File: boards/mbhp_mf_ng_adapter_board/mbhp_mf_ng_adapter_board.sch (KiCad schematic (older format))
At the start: 12 parts, among them J1 Analog Inputs, J2 Power, U1 NodeMCU_ESP32, U2 MCP3208, U3 PIC18FAdapter

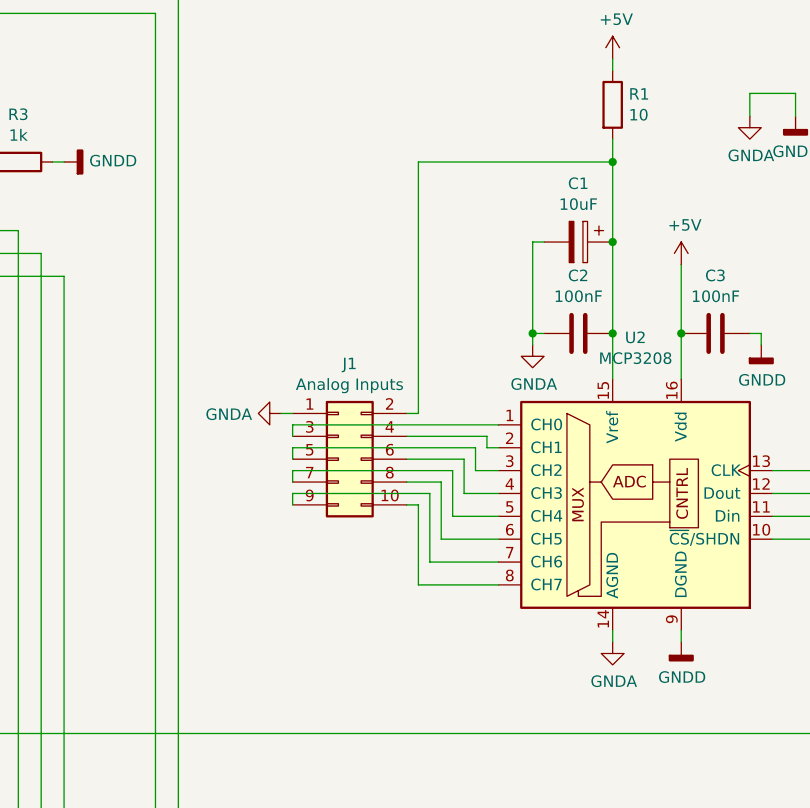
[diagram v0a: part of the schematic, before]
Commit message: Adaptor prototype ready for OSHpark
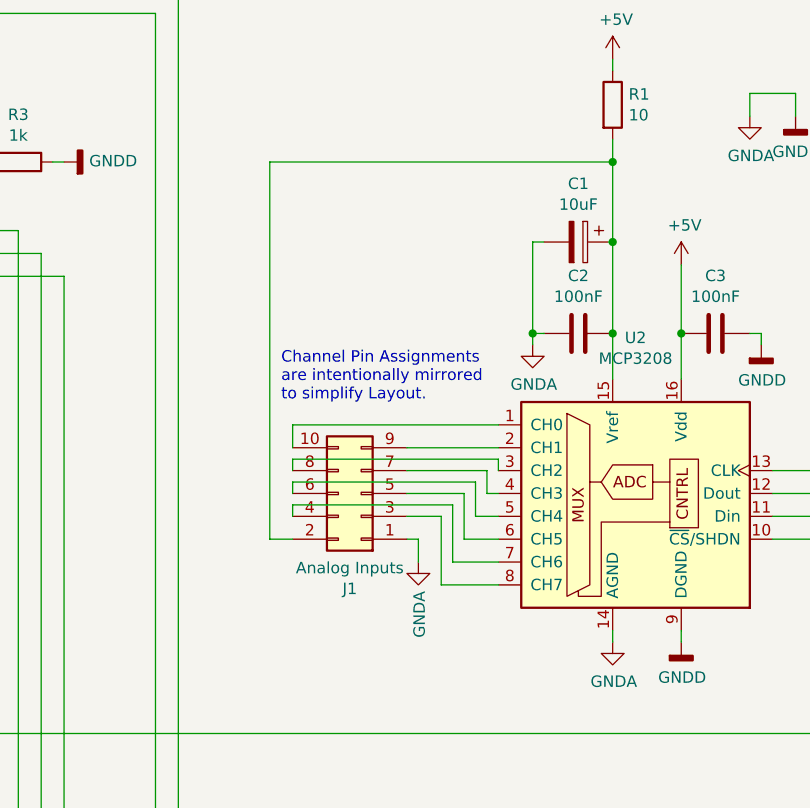
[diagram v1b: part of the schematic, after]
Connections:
- net at U2.1 (CH0): now also J1.10 (Pin_10); no longer J1.3 (Pin_3)
- net at U2.2 (CH1): now also J1.9 (Pin_9); no longer J1.4 (Pin_4)
- net at U2.3 (CH2): now also J1.8 (Pin_8); no longer J1.5 (Pin_5)
- net at U2.4 (CH3): now also J1.7 (Pin_7); no longer J1.6 (Pin_6)
- net at U2.5 (CH4): now also J1.6 (Pin_6); no longer J1.7 (Pin_7)
- net at U2.6 (CH5): now also J1.5 (Pin_5); no longer J1.8 (Pin_8)
- net at U2.7 (CH6): now also J1.4 (Pin_4); no longer J1.9 (Pin_9)
- net at U2.8 (CH7): now also J1.3 (Pin_3); no longer J1.10 (Pin_10)
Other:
- note added: "Channel Pin Assignments\nare intentionally mirrored\nto simplify Layout."
- moved on the sheet: J1
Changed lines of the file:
@@
 Text Label 4450 4050 0    50   ~ 0
 SPI_MISO_DINSR
-Wire Wire Line
-	7550 3150 7550 3500
-Wire Wire Line
-	7500 3150 7550 3150
-Wire Wire Line
-	7600 3100 7600 3400
-Wire Wire Line
-	7000 3100 7600 3100
-Wire Wire Line
-	7000 3150 7000 3100
-Wire Wire Line
-	7650 3050 7650 3300
-Wire Wire Line
-	7500 3050 7650 3050
-Wire Wire Line
-	7700 3000 7700 3200
-Wire Wire Line
-	7000 3000 7700 3000
-Wire Wire Line
-	7000 3050 7000 3000
-Wire Wire Line
-	7750 2950 7750 3100
-Wire Wire Line
-	7500 2950 7750 2950
-Wire Wire Line
-	7800 2900 7800 3000
-Wire Wire Line
-	7000 2900 7800 2900
-Wire Wire Line
-	7000 2950 7000 2900
-Wire Wire Line
-	7500 2850 7850 2850
-Wire Wire Line
-	7000 2800 7000 2850
 $Comp
 L Connector_Generic:Conn_02x05_Odd_Even J1
 U 1 1 5E140616
-P 7200 2950
-F 0 "J1" H 7250 3367 50  0000 C CNN
-F 1 "Analog Inputs" H 7250 3276 50  0000 C CNN
-F 2 "Connector_IDC:IDC-Header_2x05_P2.54mm_Vertical" H 7200 2950 50  0001 C CNN
-F 3 "~" H 7200 2950 50  0001 C CNN
-	1    7200 2950
-	1    0    0    -1
+P 7300 3100
+F 0 "J1" H 7350 3517 50  0000 C CNN
+F 1 "Analog Inputs" H 7350 3426 50  0000 C CNN
+F 2 "Connector_IDC:IDC-Header_2x05_P2.54mm_Vertical" H 7300 3100 50  0001 C CNN
+F 3 "~" H 7300 3100 50  0001 C CNN
+	1    7300 3100
+	-1   0    0    1
 $EndComp
 $Comp
 L power:GNDA #PWR01
 U 1 1 5E142455
-P 6950 2750
-F 0 "#PWR01" H 6950 2500 50  0001 C CNN
-F 1 "GNDA" V 6955 2623 50  0000 R CNN
-F 2 "" H 6950 2750 50  0001 C CNN
-F 3 "" H 6950 2750 50  0001 C CNN
-	1    6950 2750
-	0    1    1    0
+P 7550 3400
+F 0 "#PWR01" H 7550 3150 50  0001 C CNN
+F 1 "GNDA" V 7555 3273 50  0000 R CNN
+F 2 "" H 7550 3400 50  0001 C CNN
+F 3 "" H 7550 3400 50  0001 C CNN
+	1    7550 3400
+	1    0    0    -1
 $EndComp
-Wire Wire Line
-	6950 2750 7000 2750
-Wire Wire Line
-	7500 2750 7550 2750
-Wire Wire Line
-	7000 2800 7900 2800
-Wire Wire Line
-	7850 2850 7850 2900
-Wire Wire Line
-	7850 2900 7900 2900
-Wire Wire Line
-	7800 3000 7900 3000
-Wire Wire Line
-	7750 3100 7900 3100
-Wire Wire Line
-	7700 3200 7900 3200
-Wire Wire Line
-	7650 3300 7900 3300
-Wire Wire Line
-	7600 3400 7900 3400
-Wire Wire Line
-	7550 3500 7900 3500
 Text GLabel 5250 4750 2    50   Input ~ 0
 MIDI_TX
@@
 Wire Wire Line
 	8400 1550 8400 1650
-Wire Wire Line
-	7550 2750 7550 1650
-Wire Wire Line
-	7550 1650 8400 1650
 Connection ~ 8400 1650
 Wire Wire Line
 	8400 1650 8400 2000
+Wire Wire Line
+	7000 2900 7000 2800
+Wire Wire Line
+	7000 2800 7900 2800
+Wire Wire Line
+	7500 2900 7900 2900
+Wire Wire Line
+	7000 3000 7000 2950
+Wire Wire Line
+	7000 2950 7900 2950
+Wire Wire Line
+	7900 2950 7900 3000
+Wire Wire Line
+	7500 3000 7850 3000
+Wire Wire Line
+	7850 3000 7850 3100
+Wire Wire Line
+	7850 3100 7900 3100
+Wire Wire Line
+	7000 3100 7000 3050
+Wire Wire Line
+	7000 3050 7800 3050
+Wire Wire Line
+	7800 3050 7800 3200
+Wire Wire Line
+	7800 3200 7900 3200
+Wire Wire Line
+	7500 3100 7750 3100
+Wire Wire Line
+	7750 3100 7750 3300
+Wire Wire Line
+	7750 3300 7900 3300
+Wire Wire Line
+	7000 3200 7000 3150
+Wire Wire Line
+	7000 3150 7700 3150
+Wire Wire Line
+	7700 3150 7700 3400
+Wire Wire Line
+	7700 3400 7900 3400
+Wire Wire Line
+	7500 3200 7650 3200
+Wire Wire Line
+	7650 3200 7650 3500
+Wire Wire Line
+	7650 3500 7900 3500
+Wire Wire Line
+	7550 3400 7550 3300
+Wire Wire Line
+	7550 3300 7500 3300
+Wire Wire Line
+	7000 3300 6900 3300
+Wire Wire Line
+	6900 3300 6900 1650
+Wire Wire Line
+	6900 1650 8400 1650
+Text Notes 6950 2700 0    50   ~ 0
+Channel Pin Assignments\nare intentionally mirrored\nto simplify Layout.
 $EndSCHEMATC
